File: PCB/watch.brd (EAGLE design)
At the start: 81.1 x 53.1 mm, 59 parts, among them IC1 ISL1209, J2 USB-MICROB, Q1 32.768 KHz, T1 BC850, U2 MKL27Z256VLH4

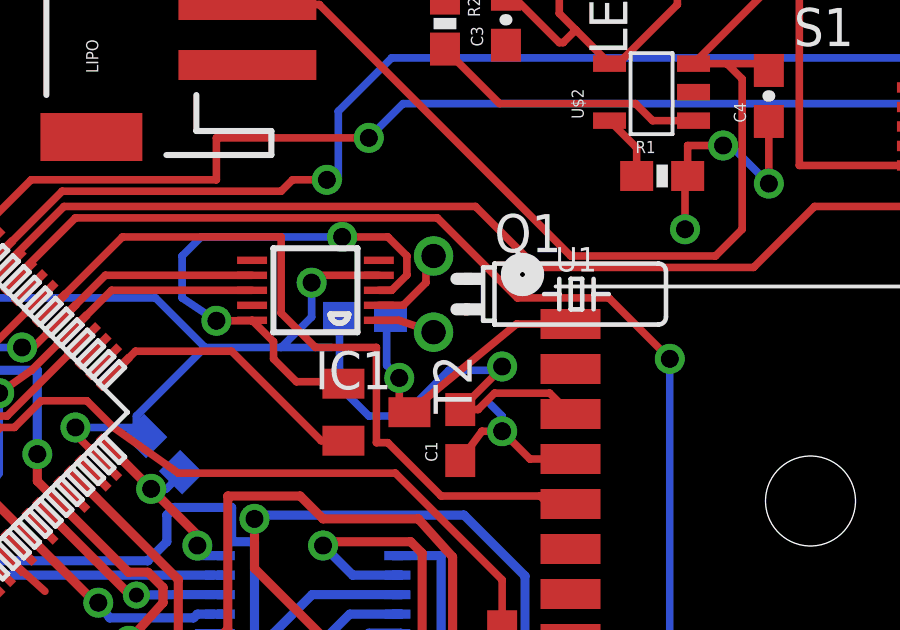
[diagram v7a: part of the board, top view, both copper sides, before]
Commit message: finished adding gps caps per https://cdn-shop.adafruit.com/datasheets/GlobalTop-FGPMMOPA6H-Datasheet-V0A.pdf page 26
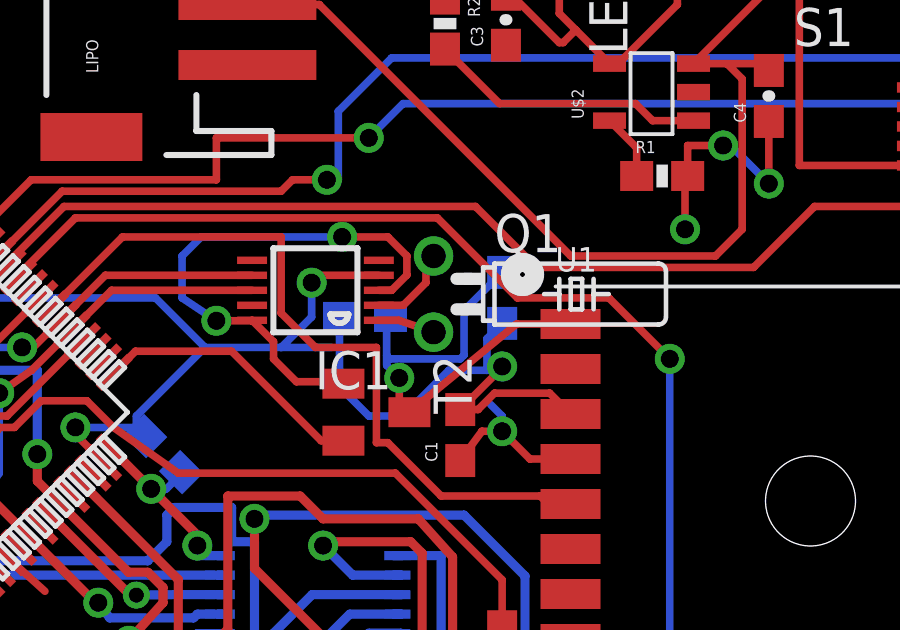
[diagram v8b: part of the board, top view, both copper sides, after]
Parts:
- added C9: .001uf, SparkFun:0603
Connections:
- net GND: now also C9.2
- net N$6: now also C9.1
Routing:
- net N$6: track 10.2 -> 16.2 mm
- net GND: track 141.1 -> 142.8 mm
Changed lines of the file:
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@@
 </element>
 <element name="GPTX" library="SparkFun-Resistors" package="0603-RES" value="330" x="70.231" y="33.909" rot="R90"/>
+<element name="C9" library="SparkFun" package="0603" value=".001uf" x="70.231" y="45.72" rot="MR270"/>
 </elements>
 <signals>
@@
 <wire x1="65.786" y1="41.783" x2="66.929" y2="41.783" width="0.254" layer="16"/>
 <wire x1="66.929" y1="41.783" x2="68.453" y2="43.307" width="0.254" layer="16"/>
-<wire x1="68.453" y1="43.307" x2="70.104" y2="43.307" width="0.254" layer="16"/>
+<wire x1="68.453" y1="43.307" x2="69.723" y2="43.307" width="0.254" layer="16"/>
+<wire x1="69.723" y1="43.307" x2="70.104" y2="43.307" width="0.254" layer="16"/>
 <wire x1="70.104" y1="43.307" x2="70.231" y2="43.434" width="0.254" layer="16"/>
 <via x="70.231" y="43.434" extent="1-16" drill="0.6"/>
@@
 <wire x1="58.039" y1="41.402" x2="58.039" y2="41.783" width="0.254" layer="16"/>
 <wire x1="58.039" y1="41.783" x2="60.325" y2="44.069" width="0.254" layer="16"/>
+<contactref element="C9" pad="2"/>
+<wire x1="70.231" y1="44.87" x2="69.723" y2="44.362" width="0.254" layer="16"/>
+<wire x1="69.723" y1="44.362" x2="69.723" y2="43.307" width="0.254" layer="16"/>
 <wire x1="63.881" y1="45.085" x2="64.809" y2="45.085" width="0" layer="19" extent="16-16"/>
 </signal>
@@
 <wire x1="66.802" y1="42.248" x2="67.14" y2="41.91" width="0.254" layer="1"/>
 <wire x1="66.382" y1="43.473" x2="66.802" y2="43.053" width="0.254" layer="16"/>
-<wire x1="66.382" y1="43.473" x2="66.382" y2="44.958" width="0.254" layer="16"/>
+<wire x1="66.382" y1="43.473" x2="66.382" y2="43.815" width="0.254" layer="16"/>
+<wire x1="66.382" y1="43.815" x2="66.382" y2="44.958" width="0.254" layer="16"/>
 <wire x1="66.382" y1="44.958" x2="66.509" y2="45.085" width="0.254" layer="16"/>
+<contactref element="C9" pad="1"/>
+<wire x1="70.231" y1="46.57" x2="68.961" y2="45.3" width="0.254" layer="16"/>
+<wire x1="68.961" y1="45.3" x2="68.961" y2="43.815" width="0.254" layer="16"/>
+<wire x1="68.961" y1="43.815" x2="68.834" y2="43.688" width="0.254" layer="16"/>
+<wire x1="68.834" y1="43.688" x2="66.509" y2="43.688" width="0.254" layer="16"/>
+<wire x1="66.509" y1="43.688" x2="66.382" y2="43.815" width="0.254" layer="16" curve="-90"/>
 </signal>
 <signal name="PTB3">
